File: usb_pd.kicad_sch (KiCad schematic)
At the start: 42 parts, among them J1 USB-C_GCT_USB4105-GF-A, J2 JST_SH_1x4_SM04B-SRSS-TB-LF-SN, Q1 SQS401EN-T1_BE3, U1 STUSB4500_QFN, U5 TVS2200DRVR, U6 TPD4E02B04DQA, U7 TVS2200DRVR, U8 TVS2200DRVR

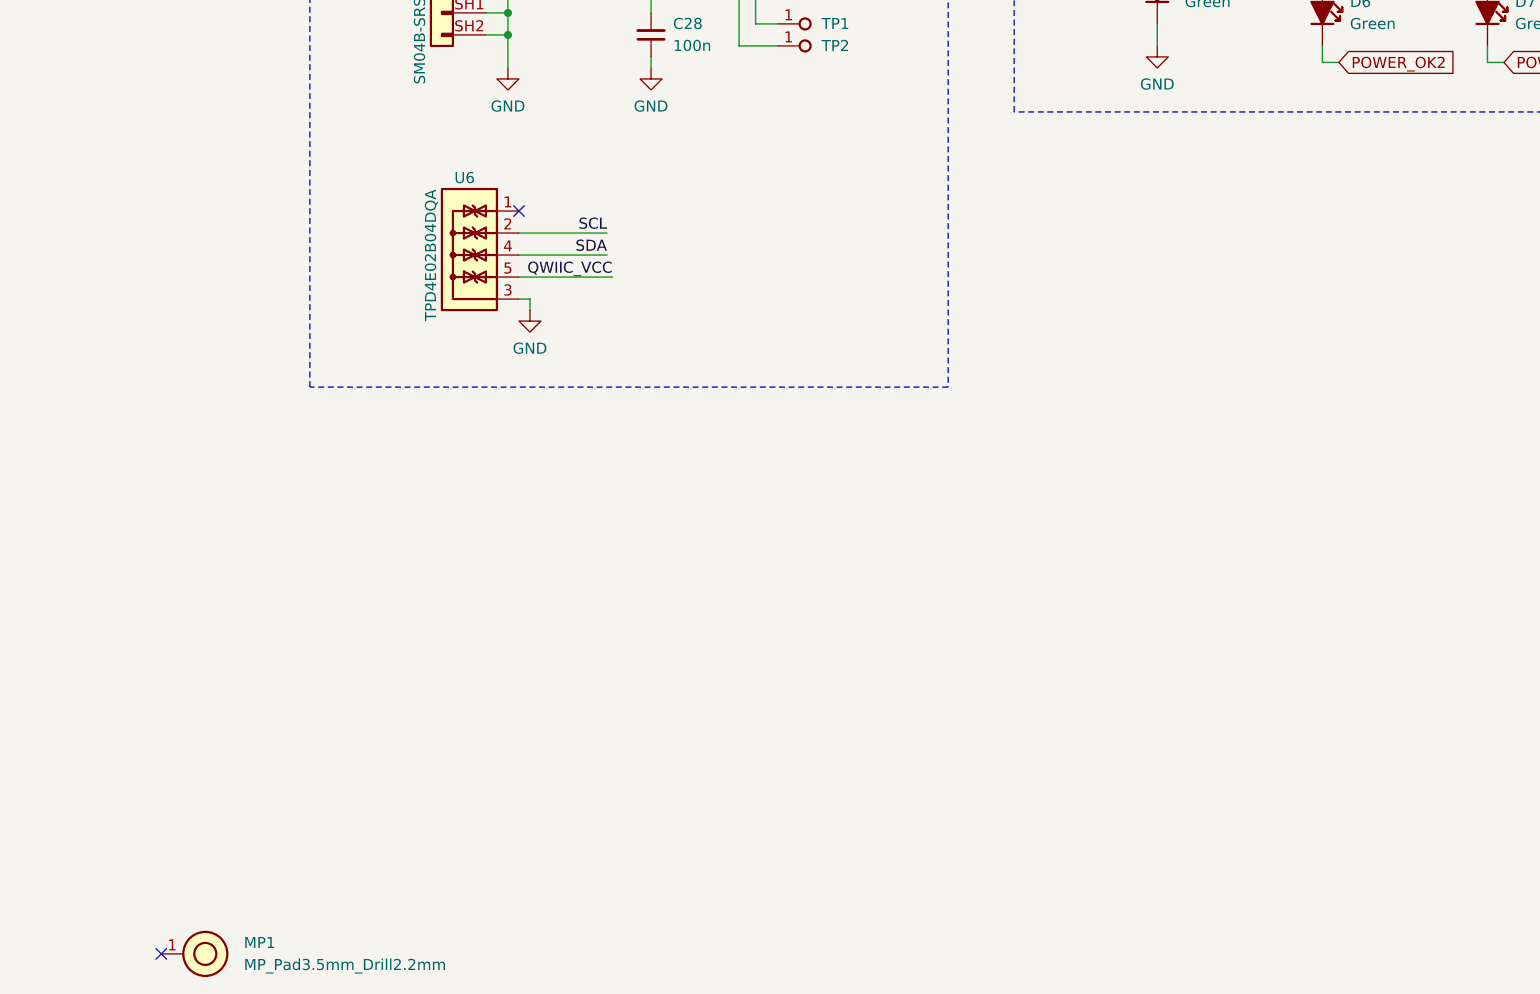
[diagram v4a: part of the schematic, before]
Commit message: [#57764] Connect MP1 to GND
Resolve DRC errors
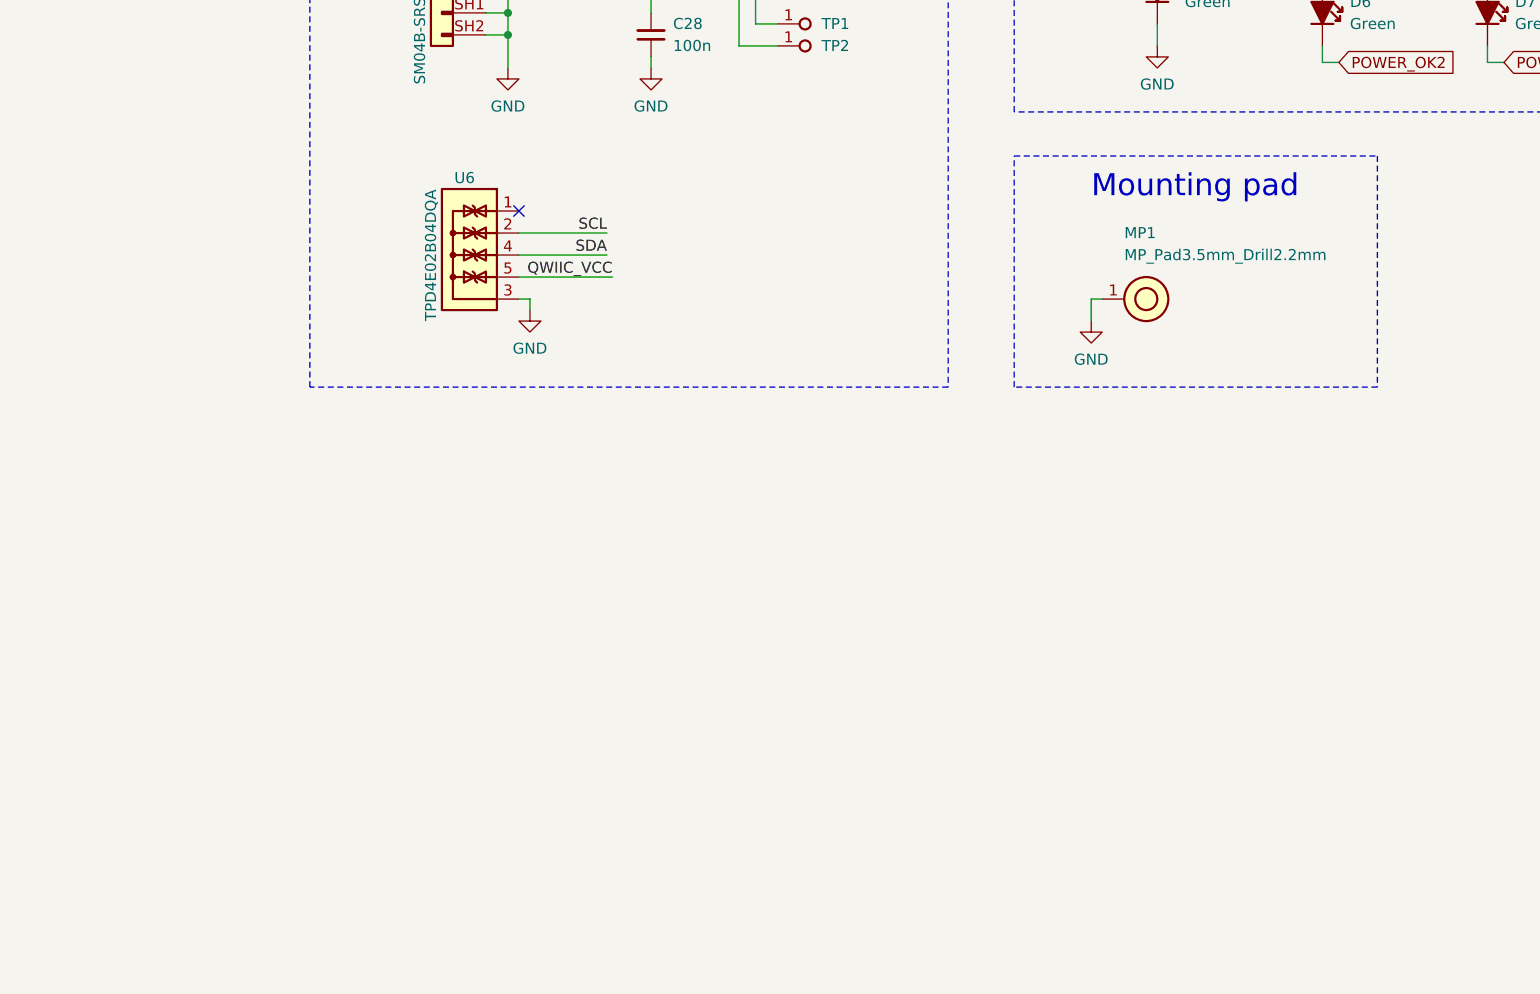
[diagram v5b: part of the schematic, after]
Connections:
- net GND: now also MP1.1
- no-connect marks 8 -> 7
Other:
- note added: "Mounting pad"
- moved on the sheet: MP1
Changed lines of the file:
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@@
   )
   (no_connect (at 66.04 66.04))
-  (no_connect (at 107.315 250.825))
   (no_connect (at 66.04 78.74))
   (no_connect (at 148.59 165.1))
@@
     (stroke (width 0) (type default))
   )
+  (wire (pts (xy 214.63 177.8) (xy 214.63 175.26))
+    (stroke (width 0) (type default))
+  )
   (wire (pts (xy 149.86 175.26) (xy 149.86 176.53))
     (stroke (width 0) (type default))
@@
     (stroke (width 0) (type default))
   )
+  (wire (pts (xy 214.63 175.26) (xy 215.9 175.26))
+    (stroke (width 0) (type default))
+  )
   (wire (pts (xy 302.26 60.96) (xy 292.1 60.96))
     (stroke (width 0) (type default))
@@
     (fill (type none))
   )
+  (rectangle (start 205.74 158.75) (end 247.65 185.42)
+    (stroke (width 0) (type dash))
+    (fill (type none))
+  )
   (rectangle (start 124.46 27.94) (end 358.14 101.6)
     (stroke (width 0) (type dash))
@@
     (effects (font (size 1.27 1.27)) (justify left bottom))
   )
+  (text "Mounting pad\n" (at 214.63 163.83 0)
+    (effects (font (size 2.54 2.54)) (justify left bottom))
+  )
   (text "QWIIC I2C Connector" (at 137.16 114.3 0)
     (effects (font (size 3 3)) (justify left bottom))
@@
     )
   )
-  (symbol (lib_id "antmicroMechanicalParts:MP_Pad3.5mm_Drill2.2mm") (at 107.315 250.825 0) (unit 1)
-    (in_bom no) (on_board yes) (dnp no) (fields_autoplaced)
-    (property "Reference" "MP1" (at 116.84 249.555 0)
+  (symbol (lib_id "antmicroMechanicalParts:MP_Pad3.5mm_Drill2.2mm") (at 215.9 175.26 0) (unit 1)
+    (in_bom no) (on_board yes) (dnp no)
+    (property "Reference" "MP1" (at 218.44 167.64 0)
       (effects (font (size 1.27 1.27) (thickness 0.15)) (justify left))
     )
-    (property "Value" "MP_Pad3.5mm_Drill2.2mm" (at 116.84 252.095 0)
+    (property "Value" "MP_Pad3.5mm_Drill2.2mm" (at 218.44 170.18 0)
       (effects (font (size 1.27 1.27) (thickness 0.15)) (justify left))
     )
-    (property "Footprint" "antmicro-footprints:MP_Pad3.5mm_Drill2.2mm" (at 122.555 260.985 0)
+    (property "Footprint" "antmicro-footprints:MP_Pad3.5mm_Drill2.2mm" (at 231.14 185.42 0)
       (effects (font (size 1.27 1.27) (thickness 0.15)) (justify left bottom) hide)
     )
-    (property "Datasheet" "" (at 124.155 266.395 0)
+    (property "Datasheet" "" (at 232.74 190.83 0)
       (effects (font (size 1.27 1.27) (thickness 0.15)) (justify left bottom) hide)
     )
-    (property "Author" "Antmicro" (at 122.555 266.065 0)
+    (property "Author" "Antmicro" (at 231.14 190.5 0)
       (effects (font (size 1.27 1.27) (thickness 0.15)) (justify left bottom) hide)
     )
-    (property "License" "Apache-2.0" (at 122.555 268.605 0)
+    (property "License" "Apache-2.0" (at 231.14 193.04 0)
       (effects (font (size 1.27 1.27) (thickness 0.15)) (justify left bottom) hide)
     )
@@
         )
       )
+    )
+  )
+  (symbol (lib_id "antmicropower:GND") (at 214.63 177.8 0) (unit 1)
+    (in_bom yes) (on_board yes) (dnp no) (fields_autoplaced)
+    (property "Reference" "#PWR03" (at 223.52 180.34 0)
+      (effects (font (size 1.27 1.27) (thickness 0.15)) (justify left bottom) hide)
+    )
+    (property "Value" "GND" (at 214.63 182.245 0)
+      (effects (font (size 1.27 1.27) (thickness 0.15)))
+    )
+    (property "Footprint" "" (at 223.52 185.42 0)
+      (effects (font (size 1.27 1.27) (thickness 0.15)) (justify left bottom) hide)
+    )
+    (property "Datasheet" "" (at 223.52 190.5 0)
+      (effects (font (size 1.27 1.27) (thickness 0.15)) (justify left bottom) hide)
+    )
+    (property "Author" "Antmicro" (at 223.52 185.42 0)
+      (effects (font (size 1.27 1.27) (thickness 0.15)) (justify left bottom) hide)
+    )
+    (property "License" "Apache-2.0" (at 223.52 187.96 0)
+      (effects (font (size 1.27 1.27) (thickness 0.15)) (justify left bottom) hide)
+    )
+    (pin "1")
+    (instances
+      (project "USB-C-power-adapter"
+        (path "/8da33aa8-79ed-467a-95ed-bf58aa0d1db6/344e016f-20ec-4e27-ac78-d9a1e9a3533b"
+          (reference "#PWR03") (unit 1)
+        )
+      )

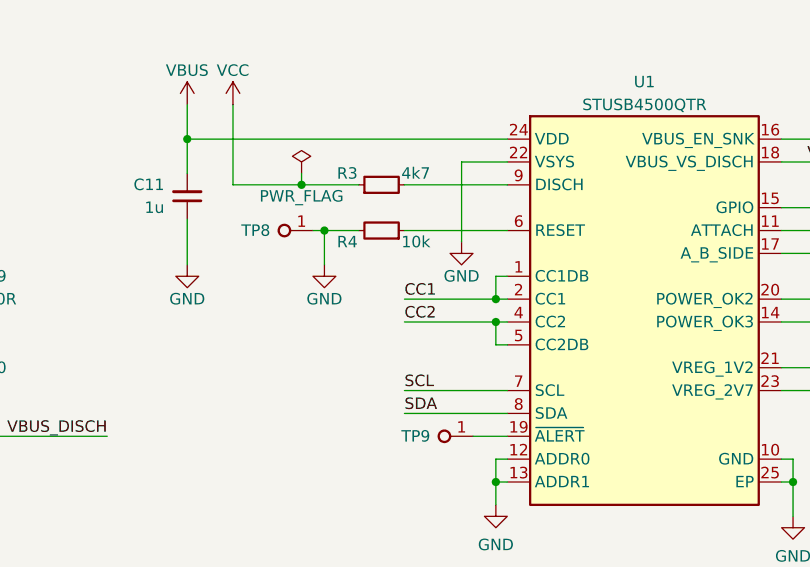
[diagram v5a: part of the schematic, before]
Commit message: [#57764] Fix TP8
Connect to RESET pin
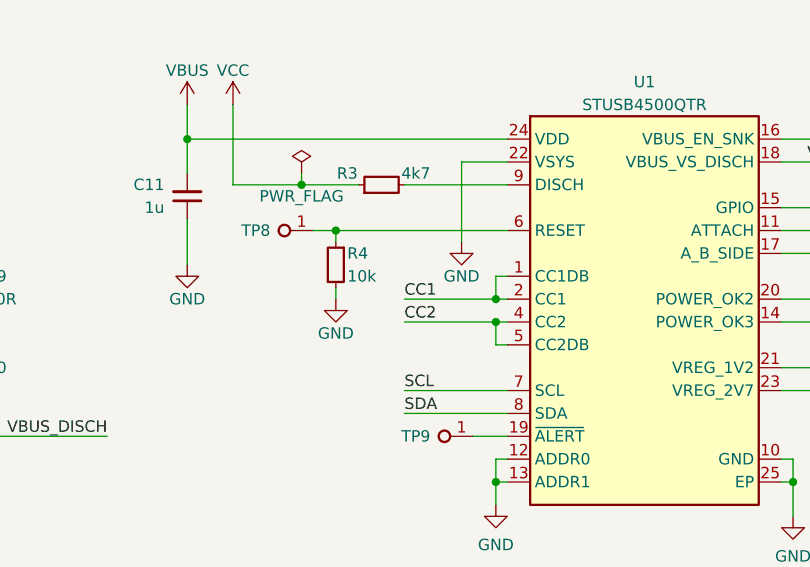
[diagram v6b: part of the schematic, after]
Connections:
- net GND: no longer TP8.1
- net at R4.1, U1.6 (RESET): now also TP8.1
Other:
- moved on the sheet: R4
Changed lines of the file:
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@@
   (junction (at 173.99 139.7) (diameter 0) (color 0 0 0 0)
   )
-  (junction (at 196.85 60.96) (diameter 0) (color 0 0 0 0)
-  )
   (junction (at 156.21 72.39) (diameter 0) (color 0 0 0 0)
   )
@@
   )
   (junction (at 179.07 137.16) (diameter 0) (color 0 0 0 0)
+  )
+  (junction (at 198.12 60.96) (diameter 0) (color 0 0 0 0)
   )
   (junction (at 304.8 73.66) (diameter 0) (color 0 0 0 0)
@@
     (stroke (width 0) (type default))
   )
-  (wire (pts (xy 196.85 60.96) (xy 196.85 64.77))
+  (wire (pts (xy 198.12 67.31) (xy 198.12 68.58))
     (stroke (width 0) (type default))
   )
@@
     (stroke (width 0) (type default))
   )
-  (wire (pts (xy 195.58 60.96) (xy 196.85 60.96))
-    (stroke (width 0) (type default))
-  )
   (wire (pts (xy 156.21 69.85) (xy 156.21 72.39))
     (stroke (width 0) (type default))
@@
     (stroke (width 0) (type default))
   )
-  (wire (pts (xy 196.85 60.96) (xy 200.66 60.96))
+  (wire (pts (xy 198.12 62.23) (xy 198.12 60.96))
     (stroke (width 0) (type default))
   )
@@
     (stroke (width 0) (type default))
   )
-  (wire (pts (xy 205.74 60.96) (xy 217.17 60.96))
+  (wire (pts (xy 198.12 60.96) (xy 217.17 60.96))
     (stroke (width 0) (type default))
   )
@@
   )
   (wire (pts (xy 146.05 72.39) (xy 146.05 69.85))
+    (stroke (width 0) (type default))
+  )
+  (wire (pts (xy 195.58 60.96) (xy 198.12 60.96))
     (stroke (width 0) (type default))
   )
@@
     )
   )
-  (symbol (lib_id "antmicroResistors0402:R_10k_0402") (at 205.74 60.96 180) (unit 1)
+  (symbol (lib_id "antmicroResistors0402:R_10k_0402") (at 198.12 62.23 270) (unit 1)
     (in_bom yes) (on_board yes) (dnp no)
-    (property "Reference" "R4" (at 199.39 62.23 0)
-      (effects (font (size 1.27 1.27) (thickness 0.15)))
-    )
-    (property "Value" "R_10k_0402" (at 185.42 48.26 0)
-      (effects (font (size 1.27 1.27) (thickness 0.15)) (justify left bottom) hide)
-    )
-    (property "Footprint" "antmicro-footprints:R_0402_1005Metric" (at 185.42 45.72 0)
-      (effects (font (size 1.27 1.27) (thickness 0.15)) (justify left bottom) hide)
-    )
-    (property "Datasheet" "https://www.bourns.com/docs/product-datasheets/cr.pdf" (at 185.42 43.18 0)
-      (effects (font (size 1.27 1.27) (thickness 0.15)) (justify left bottom) hide)
-    )
-    (property "MPN" "CR0402-FX-1002GLF" (at 185.42 40.64 0)
-      (effects (font (size 1.27 1.27) (thickness 0.15)) (justify left bottom) hide)
-    )
-    (property "Manufacturer" "Bourns" (at 185.42 38.1 0)
-      (effects (font (size 1.27 1.27) (thickness 0.15)) (justify left bottom) hide)
-    )
-    (property "License" "Apache-2.0" (at 185.42 35.56 0)
-      (effects (font (size 1.27 1.27) (thickness 0.15)) (justify left bottom) hide)
-    )
-    (property "Author" "Antmicro" (at 185.42 33.02 0)
-      (effects (font (size 1.27 1.27) (thickness 0.15)) (justify left bottom) hide)
-    )
-    (property "Val" "10k" (at 207.01 62.23 0)
-      (effects (font (size 1.27 1.27) (thickness 0.15)))
-    )
-    (property "Tolerance" "1%" (at 185.42 50.8 0)
+    (property "Reference" "R4" (at 199.39 63.5 90)
+      (effects (font (size 1.27 1.27) (thickness 0.15)) (justify left))
+    )
+    (property "Value" "R_10k_0402" (at 185.42 82.55 0)
+      (effects (font (size 1.27 1.27) (thickness 0.15)) (justify left bottom) hide)
+    )
+    (property "Footprint" "antmicro-footprints:R_0402_1005Metric" (at 182.88 82.55 0)
+      (effects (font (size 1.27 1.27) (thickness 0.15)) (justify left bottom) hide)
+    )
+    (property "Datasheet" "https://www.bourns.com/docs/product-datasheets/cr.pdf" (at 180.34 82.55 0)
+      (effects (font (size 1.27 1.27) (thickness 0.15)) (justify left bottom) hide)
+    )
+    (property "MPN" "CR0402-FX-1002GLF" (at 177.8 82.55 0)
+      (effects (font (size 1.27 1.27) (thickness 0.15)) (justify left bottom) hide)
+    )
+    (property "Manufacturer" "Bourns" (at 175.26 82.55 0)
+      (effects (font (size 1.27 1.27) (thickness 0.15)) (justify left bottom) hide)
+    )
+    (property "License" "Apache-2.0" (at 172.72 82.55 0)
+      (effects (font (size 1.27 1.27) (thickness 0.15)) (justify left bottom) hide)
+    )
+    (property "Author" "Antmicro" (at 170.18 82.55 0)
+      (effects (font (size 1.27 1.27) (thickness 0.15)) (justify left bottom) hide)
+    )
+    (property "Val" "10k" (at 199.39 66.04 90)
+      (effects (font (size 1.27 1.27) (thickness 0.15)) (justify left))
+    )
+    (property "Tolerance" "1%" (at 187.96 82.55 0)
       (effects (font (size 1.27 1.27)) (justify left bottom) hide)
     )
@@
     )
   )
-  (symbol (lib_id "antmicropower:GND") (at 196.85 64.77 0) (unit 1)
+  (symbol (lib_id "antmicropower:GND") (at 198.12 68.58 0) (unit 1)
     (in_bom yes) (on_board yes) (dnp no)
-    (property "Reference" "#PWR087" (at 205.74 67.31 0)
-      (effects (font (size 1.27 1.27) (thickness 0.15)) (justify left bottom) hide)
-    )
-    (property "Value" "GND" (at 196.85 68.58 0)
+    (property "Reference" "#PWR087" (at 207.01 71.12 0)
+      (effects (font (size 1.27 1.27) (thickness 0.15)) (justify left bottom) hide)
+    )
+    (property "Value" "GND" (at 198.12 72.39 0)
       (effects (font (size 1.27 1.27) (thickness 0.15)))
     )
-    (property "Footprint" "" (at 205.74 72.39 0)
-      (effects (font (size 1.27 1.27) (thickness 0.15)) (justify left bottom) hide)
-    )
-    (property "Datasheet" "" (at 205.74 77.47 0)
-      (effects (font (size 1.27 1.27) (thickness 0.15)) (justify left bottom) hide)
-    )
-    (property "Author" "Antmicro" (at 205.74 72.39 0)
-      (effects (font (size 1.27 1.27) (thickness 0.15)) (justify left bottom) hide)
-    )
-    (property "License" "Apache-2.0" (at 205.74 74.93 0)
-      (effects (font (size 1.27 1.27) (thickness 0.15)) (justify left bottom) hide)
-    )
+    (property "Footprint" "" (at 207.01 76.2 0)
+      (effects (font (size 1.27 1.27) (thickness 0.15)) (justify left bottom) hide)
+    )
+    (property "Datasheet" "" (at 207.01 81.28 0)
+      (effects (font (size 1.27 1.27) (thickness 0.15)) (justify left bottom) hide)
+    )
+    (property "Author" "Antmicro" (at 207.01 76.2 0)
+      (effects (font (size 1.27 1.27) (thickness 0.15)) (justify left bottom) hide)
+    )
+    (property "License" "Apache-2.0" (at 207.01 78.74 0)
+      (effects (font (size 1.27 1.27) (thickness 0.15)) (justify left bottom) hide)
+    )
